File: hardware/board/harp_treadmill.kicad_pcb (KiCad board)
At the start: 4 copper layers, 80 x 100 mm, 164 parts, among them J1 Conn_01x03_Male, J2 AudioJack3, J3 Conn_01x05_Female, J4 Conn_01x02_Female, J5 USB_C_Receptacle_USB2.0, J6 Barrel_Jack_Switch, J7 Conn_01x04_Female, Q2 Si7336ADP, U1 LP2985-3.3, U10 AD8615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

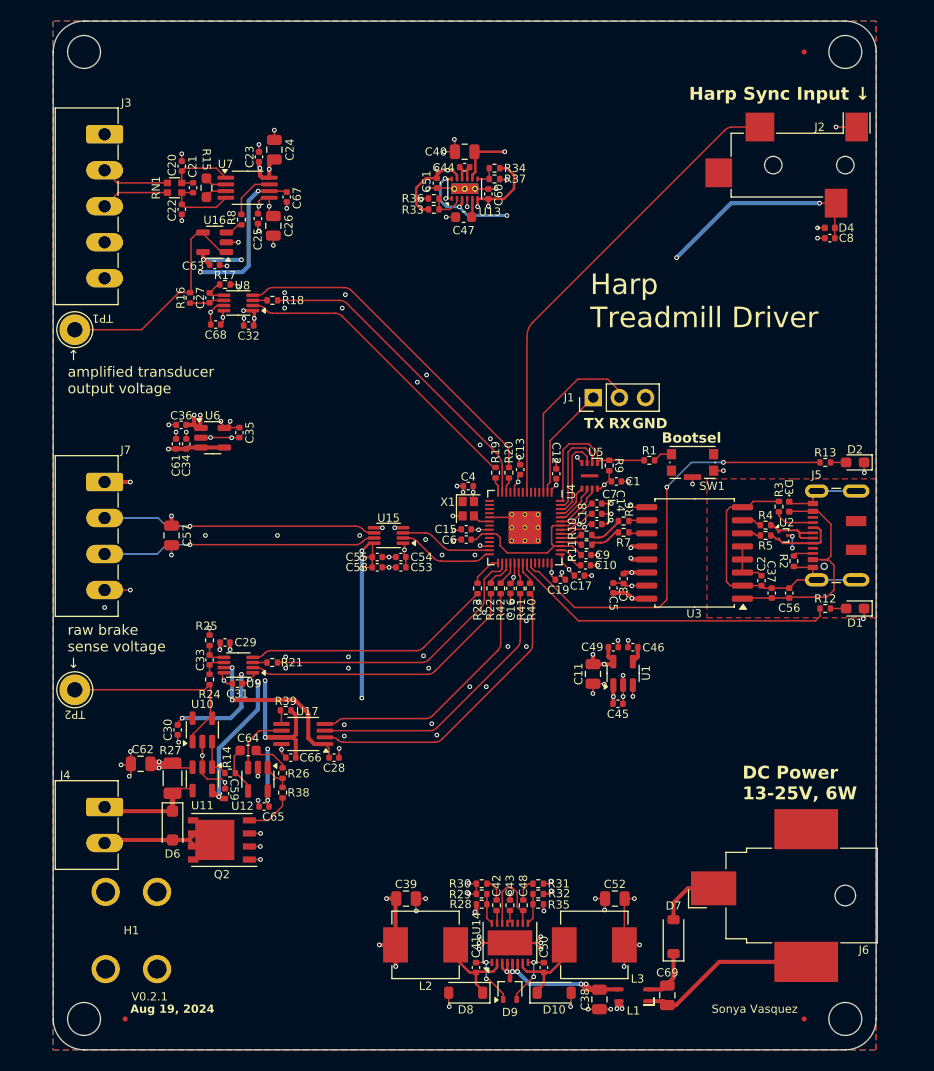
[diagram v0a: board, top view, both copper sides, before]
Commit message: add tvs diodes to inputs
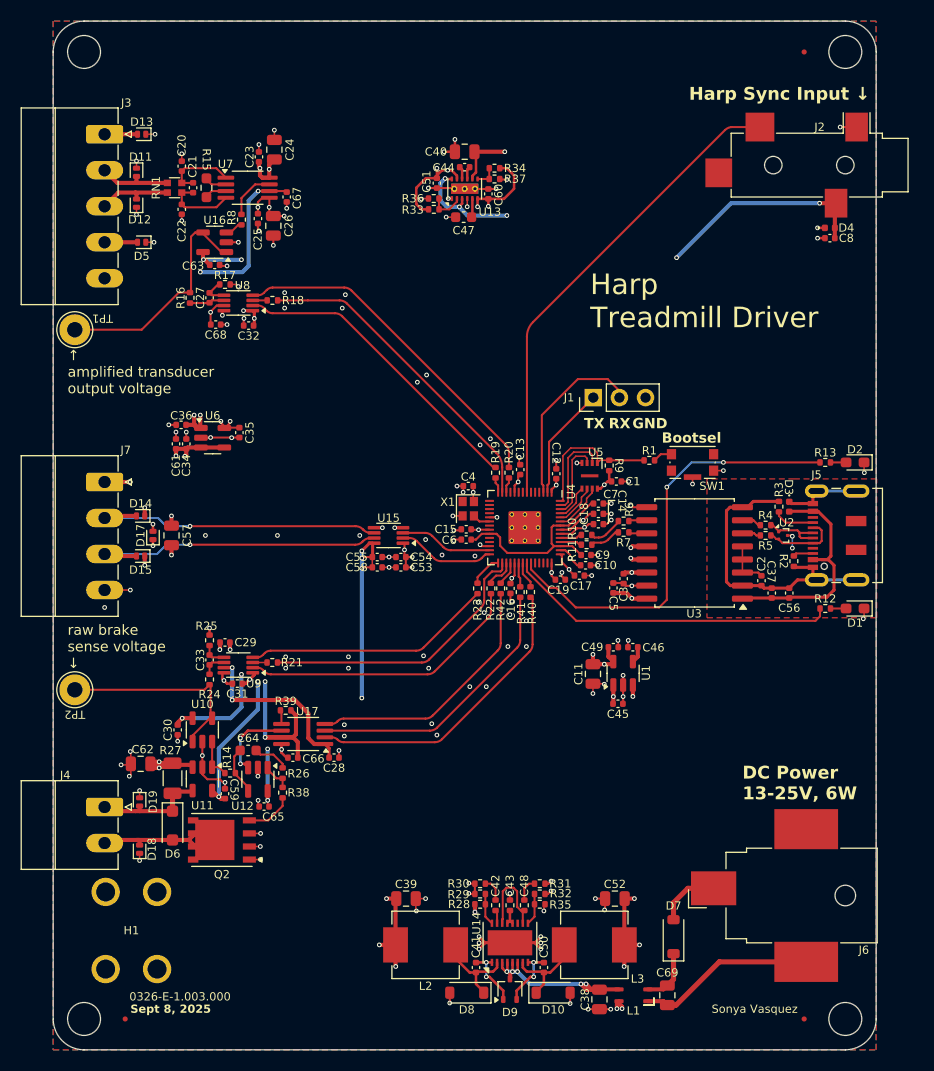
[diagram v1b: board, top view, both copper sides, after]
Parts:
- added D11: D_TVS, Diode_SMD:D_SOD-882D, F.Cu at (108.1, 44.7)
- added D12: D_TVS, Diode_SMD:D_SOD-882D, F.Cu at (108.1, 47.7)
- added D13: D_TVS, Diode_SMD:D_SOD-882D, F.Cu at (108.6, 41.0)
- added D14: D_TVS, Diode_SMD:D_SOD-882D, F.Cu at (108.5, 78.1)
- added D15: D_TVS, Diode_SMD:D_SOD-882D, F.Cu at (108.5, 82.0)
- added D17: D_TVS, Diode_SMD:D_SOD-882D, F.Cu at (109.7, 80.0)
- added D18: D_TVS, Diode_SMD:D_SOD-882D, F.Cu at (108.4, 110.5)
- added D19: D_TVS, Diode_SMD:D_SOD-882D, F.Cu at (108.4, 105.9)
- added D5: D_TVS, Diode_SMD:D_SOD-882D, F.Cu at (108.6, 51.5)
- moved R40 0.35 mm to (146.4, 85.5)
- moved R41 0.35 mm to (145.4, 85.5)
- moved C66 0.20 mm to (123.3, 101.6)
- moved C14 0.15 mm to (153.0, 78.9)
- moved C18 0.15 mm to (153.0, 77.9)
- moved C7 0.15 mm to (153.0, 76.9)
- moved R28 0.15 mm to (141.5, 115.8)
- moved R29 0.15 mm to (141.5, 114.8)
- moved R30 0.15 mm to (141.5, 113.8)
- moved R31 0.15 mm to (147.3, 113.8)
- moved R32 0.15 mm to (147.3, 114.8)
- moved R35 0.15 mm to (147.3, 115.8)
- moved C48 0.10 mm to (145.8, 116.0)
- moved C42 0.10 mm to (143.0, 116.0)
- moved D10 0.10 mm to (148.6, 124.5)
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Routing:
- net -5V: track 13.0 -> 17.2 mm, vias 4 -> 5
- net Net-(D14-A2): track 26.6 -> 29.7 mm
- net Net-(D15-A2): track 26.6 -> 29.8 mm
- net +5V: track 14.2 -> 16.9 mm
- net GND: track 120.8 -> 122.9 mm, vias 134 -> 145
- net Net-(D18-A2): track 9.92 -> 11.7 mm
- net 5V2: track 65.1 -> 66.6 mm, vias 19 -> 21
- net Net-(U12-+): track 6.20 -> 7.69 mm, vias 0 -> 2
- net +3V3: track 115.2 -> 116.5 mm, vias 32 -> 34
- net Net-(D11-A2): track 6.61 -> 7.44 mm
- net Net-(D12-A2): track 6.65 -> 7.32 mm
- net /Harp Core RP2040 + Isolated USB/QSPI_CS: track 14.7 -> 14.1 mm
- net /Harp Core RP2040 + Isolated USB/QSPI_D1: track 9.29 -> 8.67 mm
- net /Harp Core RP2040 + Isolated USB/QSPI_D2: track 8.32 -> 7.70 mm
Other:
- board text added: "0326-E-1.003.000"
- board text added: "Sept 8, 2025"
- board text removed: "Aug 19, 2024"
- board text removed: "V0.2.1"
